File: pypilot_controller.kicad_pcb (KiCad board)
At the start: 4 copper layers, 76.6 x 50.6 mm, 99 parts, among them J1 power+, J10 Clutch, J2 power-, J3 Motor A, J4 Motor B, J5 UART_Device, J6 Rudder, J7 End Stops, J8 Conn_01x02, J9 ISP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

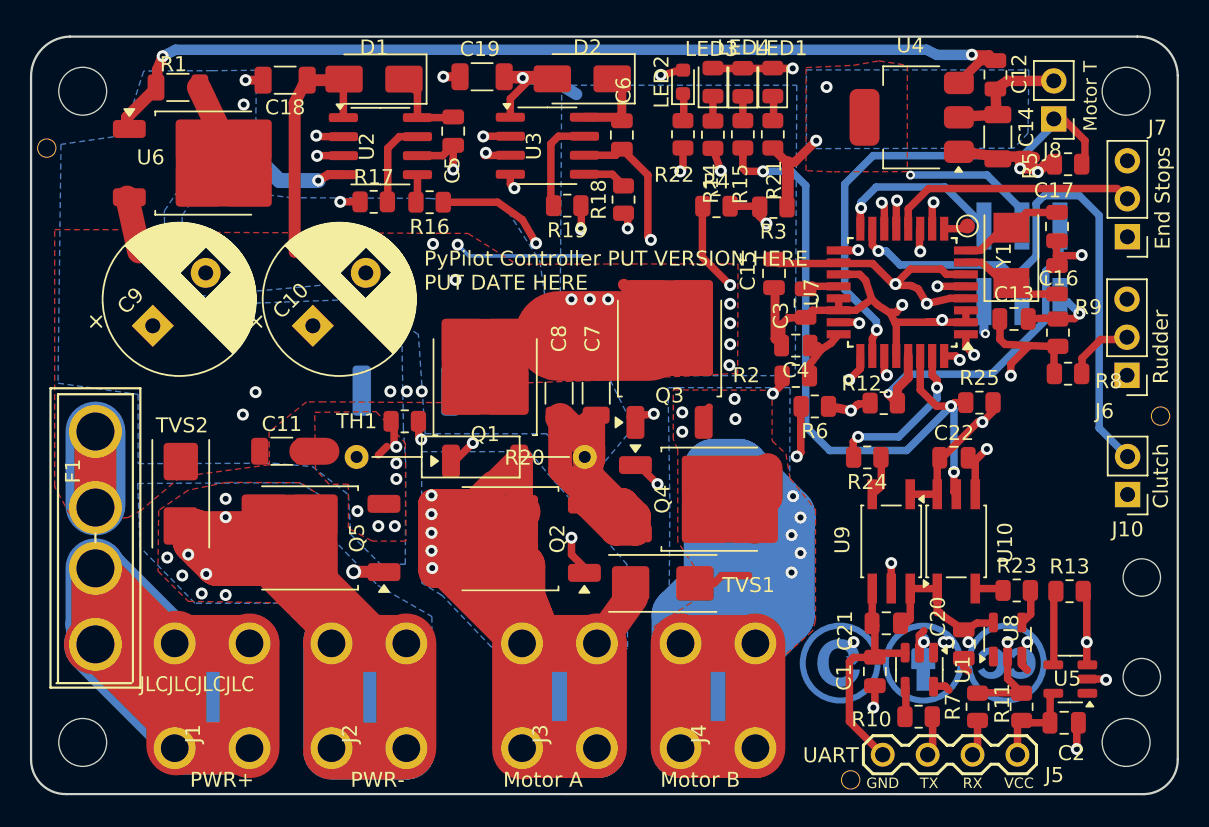
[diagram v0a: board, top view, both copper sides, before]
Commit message: Change TO-252 footprint to use less solder paste
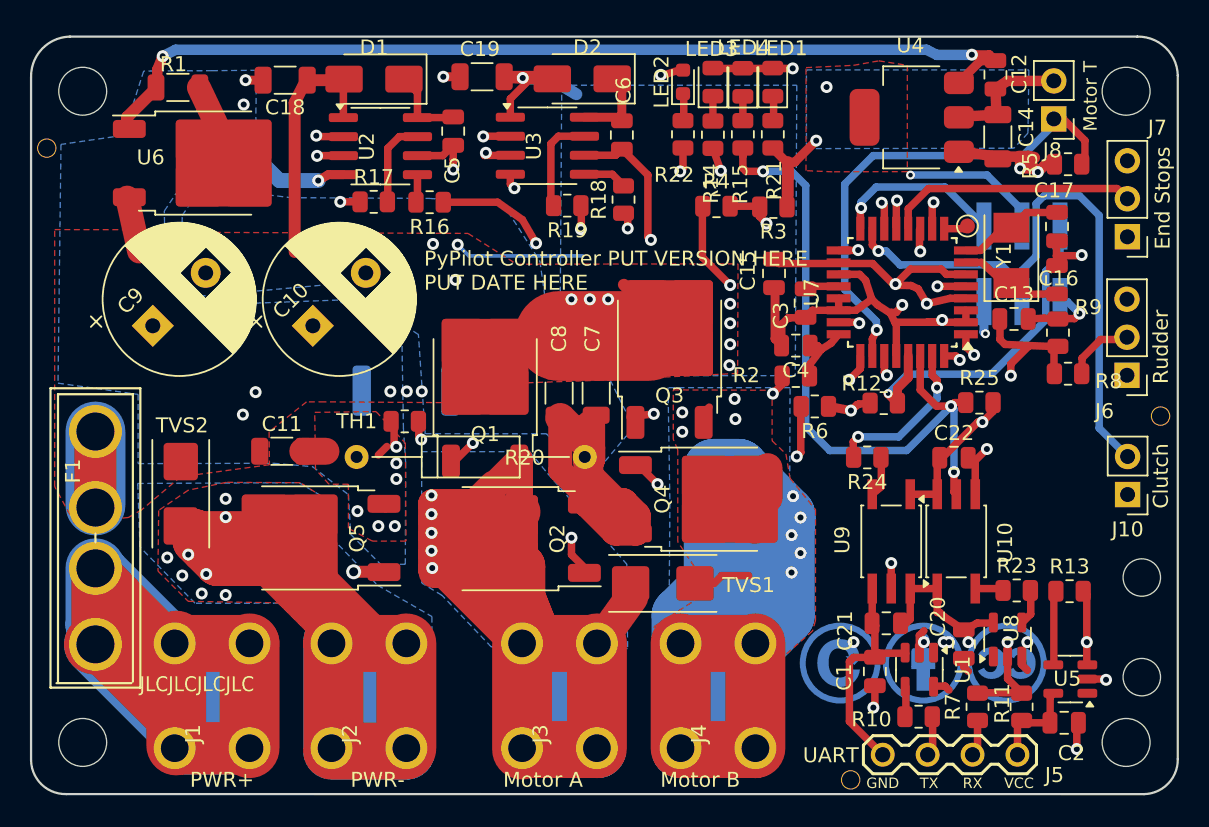
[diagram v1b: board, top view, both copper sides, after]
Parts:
- Q1, Q2, Q3, Q4, Q5, U6: footprint Package_TO_SOT_SMD:TO-252-2 -> pypilot_controller_footprints:TO-252-2-reduced-paste

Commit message: Cleaned up designators - where possible, they are all right way up
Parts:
- moved C12 0.79 mm to (66.3, 4.30)
- moved C14 0.76 mm to (66.4, 8.40)
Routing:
- net +5V: track 122.1 -> 118.3 mm
- net Net-(U4-VI): track 65.2 -> 67.1 mm
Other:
- board text added: "5V"
- board text added: "CK"
- board text added: "RX"
- board text added: "TX"

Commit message: Added license tag and moved eye candy on reverse side around
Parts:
- moved REF** 16.7 mm to (66.6, 35.8)
- moved REF** 6.41 mm to (55.3, 36.0)
- moved REF** 1.70 mm to (56.0, 44.5)
- moved REF** 1.70 mm to (61.6, 44.5)
- moved REF** 1.70 mm to (67.1, 44.5)
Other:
- board text added: "CC-BY-SA v4.0"
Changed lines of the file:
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@@
 	(footprint "Symbol:Symbol_CC-ShareAlike_CopperTop_Small"
 		(layer "B.Cu")
-		(at 55.9 42.8 180)
+		(at 56 44.5 180)
 		(descr "Creative Commons symbol, CC-SA, copper layer, 5mm")
 		(tags "share-alike license graphic")
@@
 	(footprint "pypilot_controller_footprints:KiCad-Logo2_6mm_SilkScreen"
 		(layer "B.Cu")
-		(at 61.707487 36.117365 180)
+		(at 55.3 36 180)
 		(descr "KiCad Logo")
 		(tags "Logo KiCad")
@@
 	(footprint "Symbol:Symbol_CreativeCommons_CopperTop_Type2_Small"
 		(layer "B.Cu")
-		(at 67 42.8 180)
+		(at 67.1 44.5 180)
 		(descr "Creative Commons symbol, CC, copper layer, 5mm")
 		(tags "license graphic")
@@
 	(footprint "Symbol:OSHW-Logo_5.7x6mm_SilkScreen"
 		(layer "B.Cu")
-		(at 49.9 35.5 180)
+		(at 66.6 35.8 180)
 		(descr "Open Source Hardware Logo")
 		(tags "Logo OSHW")
@@
 	(footprint "Symbol:Symbol_CC-Attribution_CopperTop_Small"
 		(layer "B.Cu")
-		(at 61.45032 42.8 180)
+		(at 61.55032 44.5 180)
 		(descr "Creative Commons symbol, CC-BY, copper layer, 5mm")
 		(property "Reference" "REF**"
@@
 			)
 			(justify left top mirror)
+		)
+	)
+	(gr_text "CC-BY-SA v4.0"
+		(at 69.5 39.7 0)
+		(layer "B.SilkS")
+		(effects
+			(font
+				(size 1 1)
+				(thickness 0.15)
+			)
+			(justify left top mirror)

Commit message: Fixed almost all ERC errors and warnings (now 0 errors, 3 warnings)
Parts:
- added NT1: NetTie_2, NetTie:NetTie-2_SMD_Pad0.5mm, B.Cu at (69.2, 13.8)
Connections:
- J10 pad 2: MOSI -> /sense/Clutch
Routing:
- net MOSI: track 42.1 -> 18.1 mm
- net /sense/Clutch: track 0.00 -> 22.9 mm
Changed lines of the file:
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@@
 	(net 59 "unconnected-(U5-Pad1)")
 	(net 60 "unconnected-(U8-Pad1)")
+	(net 61 "/sense/Clutch")
 	(footprint "Resistor_SMD:R_0805_2012Metric"
 		(layer "F.Cu")
@@
 			(layers "*.Cu" "*.Mask")
 			(remove_unused_layers no)
-			(net 10 "MOSI")
+			(net 61 "/sense/Clutch")
 			(pinfunction "Pin_2")
 			(pintype "passive")
@@
 		)
 	)
+	(footprint "NetTie:NetTie-2_SMD_Pad0.5mm"
+		(layer "B.Cu")
+		(at 69.2 13.8 90)
+		(descr "Net tie, 2 pin, 0.5mm square SMD pads")
+		(tags "net tie")
+		(property "Reference" "NT1"
+			(at 0 1.2 90)
+			(layer "B.SilkS")
+			(hide yes)
+			(effects
+				(font
+					(size 1 1)
+					(thickness 0.15)
+				)
+				(justify mirror)
+			)
+		)
+		(property "Value" "NetTie_2"
+			(at 0 -1.2 90)
+			(layer "B.Fab")
+			(hide yes)
+			(effects
+				(font
+					(size 1 1)
+					(thickness 0.15)
+				)
+				(justify mirror)
+			)
+		)
+		(property "Footprint" "NetTie:NetTie-2_SMD_Pad0.5mm"
+			(at 0 0 -90)
+			(unlocked yes)
+			(layer "B.Fab")
+			(hide yes)
+			(effects
+				(font
+					(size 1.27 1.27)
+					(thickness 0.15)
+				)
+				(justify mirror)
+			)
+		)
+		(property "Datasheet" ""
+			(at 0 0 -90)
+			(unlocked yes)
+			(layer "B.Fab")
+			(hide yes)
+			(effects
+				(font
+					(size 1.27 1.27)
+					(thickness 0.15)
+				)
+				(justify mirror)
+			)
+		)
+		(property "Description" "Net tie, 2 pins"
+			(at 0 0 -90)
+			(unlocked yes)
+			(layer "B.Fab")
+			(hide yes)
+			(effects
+				(font
+					(size 1.27 1.27)
+					(thickness 0.15)
+				)
+				(justify mirror)
+			)
+		)
+		(property ki_fp_filters "Net*Tie*")
+		(sheetname "sense")
+		(sheetfile "sense.kicad_sch")
+		(attr exclude_from_pos_files exclude_from_bom allow_missing_courtyard)
+		(net_tie_pad_groups "1, 2")
+		(fp_poly
+			(pts
+				(xy -0.5 0.25) (xy 0.5 0.25) (xy 0.5 -0.25) (xy -0.5 -0.25)
+			)
+			(stroke
+				(width 0)
+				(type solid)
+			)
+			(fill solid)
+			(layer "B.Cu")
+		)
+		(pad "1" smd circle
+			(at -0.5 0 90)
+			(size 0.5 0.5)
+			(layers "B.Cu")
+			(net 10 "MOSI")
+			(pinfunction "1")
+			(pintype "passive")
+		)
+		(pad "2" smd circle
+			(at 0.5 0 90)
+			(size 0.5 0.5)
+			(layers "B.Cu")
+			(net 61 "/sense/Clutch")
+			(pinfunction "2")
+			(pintype "passive")
+		)
+	)
 	(footprint "Resistor_SMD:R_2512_6332Metric"
 		(layer "B.Cu")
@@
 	)
 	(segment
-		(start 71.875 11.575)
-		(end 73.2 12.9)
-		(width 0.5)
-		(layer "B.Cu")
-		(net 10)
-	)
-	(segment
 		(start 68.04 17.575)
 		(end 68.04 18.65)
@@
 	)
 	(segment
-		(start 68.99 15.625)
-		(end 68.99 12.11)
-		(width 0.5)
-		(layer "B.Cu")
-		(net 10)
-	)
-	(segment
 		(start 66.665 16.2)
 		(end 68.04 17.575)
@@
 	)
 	(segment
-		(start 68.04 16.575)
-		(end 68.99 15.625)
-		(width 0.5)
-		(layer "B.Cu")
-		(net 10)
-	)
-	(segment
 		(start 58.454899 15.274501)
 		(end 58.974501 15.274501)
@@
 	)
 	(segment
-		(start 69.525 11.575)
-		(end 71.875 11.575)
-		(width 0.5)
-		(layer "B.Cu")
-		(net 10)
-	)
-	(segment
-		(start 73.2 27.1)
-		(end 75.1 29)
+		(start 69.2 15.415)
+		(end 69.2 14.3)
 		(width 0.5)
 		(layer "B.Cu")
@@
 	)
 	(segment
-		(start 68.99 12.11)
-		(end 69.525 11.575)
+		(start 68.04 16.575)
+		(end 69.2 15.415)
 		(width 0.5)
 		(layer "B.Cu")
@@
 	)
 	(segment
-		(start 73.2 12.9)
-		(end 73.2 27.1)
-		(width 0.5)
-		(layer "B.Cu")
-		(net 10)
-	)
-	(segment
 		(start 58.974501 15.274501)
 		(end 59.9 16.2)
@@
 		(net 57)
 	)
+	(segment
+		(start 75.1 29)
+		(end 73.2 27.1)
+		(width 0.5)
+		(layer "B.Cu")
+		(net 61)
+	)
+	(segment
+		(start 69.2 12.005)
+		(end 69.2 13.3)
+		(width 0.5)
+		(layer "B.Cu")
+		(net 61)
+	)
+	(segment
+		(start 71.875 11.575)
+		(end 69.63 11.575)
+		(width 0.5)
+		(layer "B.Cu")
+		(net 61)
+	)
+	(segment
+		(start 73.2 27.1)
+		(end 73.2 12.9)
+		(width 0.5)
+		(layer "B.Cu")
+		(net 61)
+	)
+	(segment
+		(start 73.2 12.9)
+		(end 71.875 11.575)
+		(width 0.5)
+		(layer "B.Cu")
+		(net 61)
+	)
+	(segment
+		(start 69.63 11.575)
+		(end 69.2 12.005)
+		(width 0.5)
+		(layer "B.Cu")
+		(net 61)
+	)
 	(zone

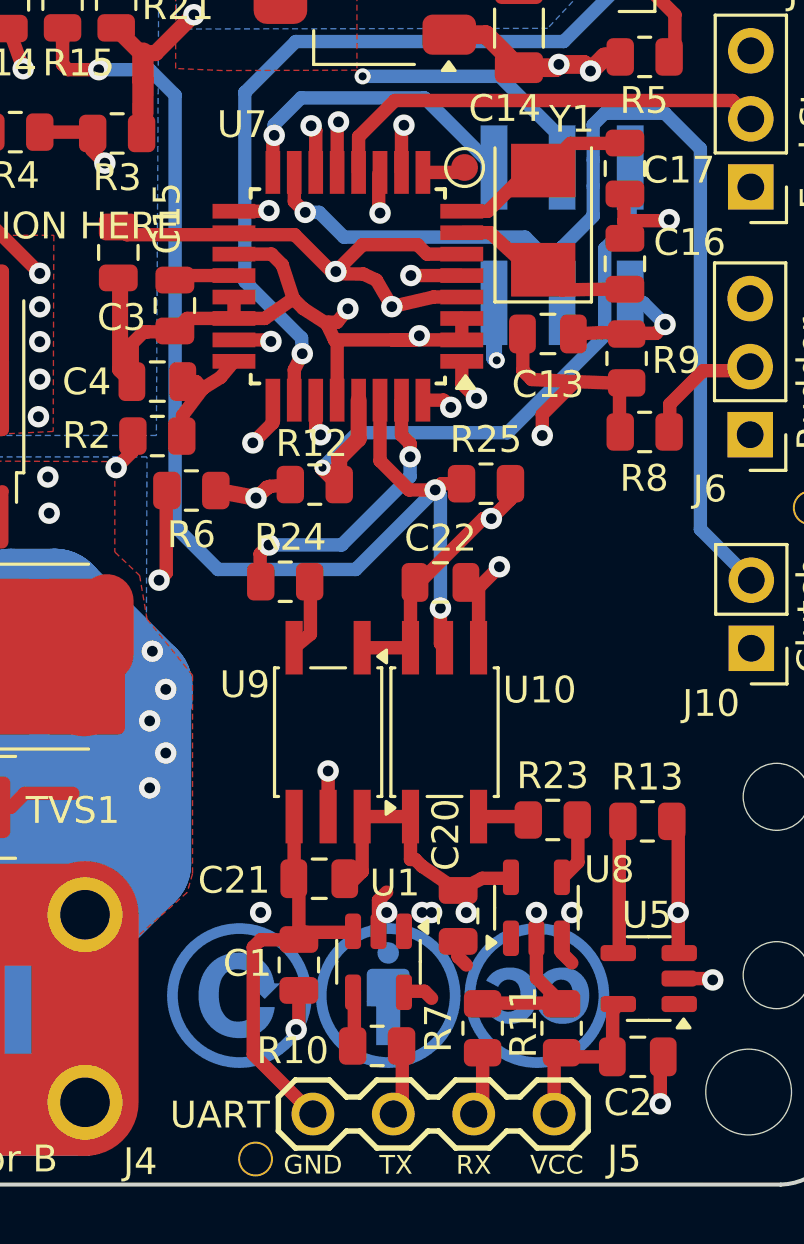
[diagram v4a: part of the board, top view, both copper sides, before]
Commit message: Fixed up some net breakage caused by the on-copper graphics on the back
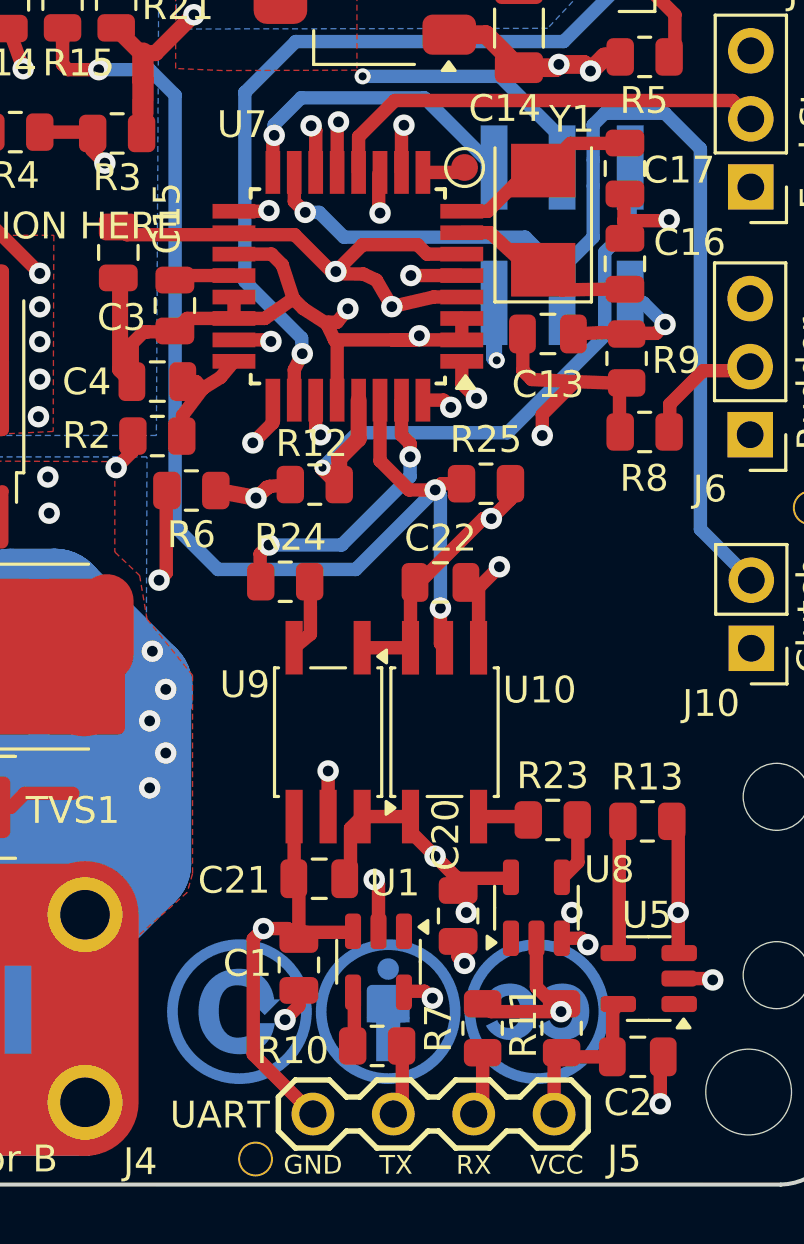
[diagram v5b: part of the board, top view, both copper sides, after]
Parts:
- moved REF** 0.60 mm to (56.0, 45.1)
- moved REF** 0.60 mm to (67.1, 45.1)
- moved REF** 0.60 mm to (61.6, 45.1)
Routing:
- net Net-(R11-Pad1): track 14.5 -> 13.6 mm
- net Net-(J5-GND): track 48.0 -> 48.8 mm, vias 4 -> 6

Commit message: Removed as many DRC errors and warnings as I could
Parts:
- removed the T2 at (56.6, 50.6)
- moved U6 2.15 mm to (15.6, 9.30)
- moved U5 1.57 mm to (71.3, 42.3)
- moved C2 0.46 mm to (70.5, 46.5), turned to 90 degrees
- moved D1 0.34 mm to (25.1, 3.79)
- moved TH1 0.15 mm to (26.8, 26.5)
- moved T1 0.10 mm to (3.00, 8.40)
- renumbered T3 to T2
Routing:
- net Net-(J5-GND): track 48.8 -> 43.7 mm, vias 6 -> 5
- net GND: track 78.6 -> 82.6 mm
- net /sense/PWMAL: track 51.9 -> 48.6 mm
- net /sense/PWMAH: track 45.0 -> 41.8 mm
- net Net-(U6-VO): track 6.69 -> 4.29 mm
- net Net-(Q1-G): track 23.5 -> 21.1 mm
- net Net-(R11-Pad1): track 13.6 -> 11.8 mm
- net Net-(J5-VCC): track 36.9 -> 38.5 mm, vias 4 -> 3
- net Net-(R13-Pad1): track 4.96 -> 3.41 mm
- net Net-(U4-VI): track 67.1 -> 66.2 mm
